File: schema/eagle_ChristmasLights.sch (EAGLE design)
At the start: 3 parts, among them SW1 FSM6JSMA, U1 WS2812

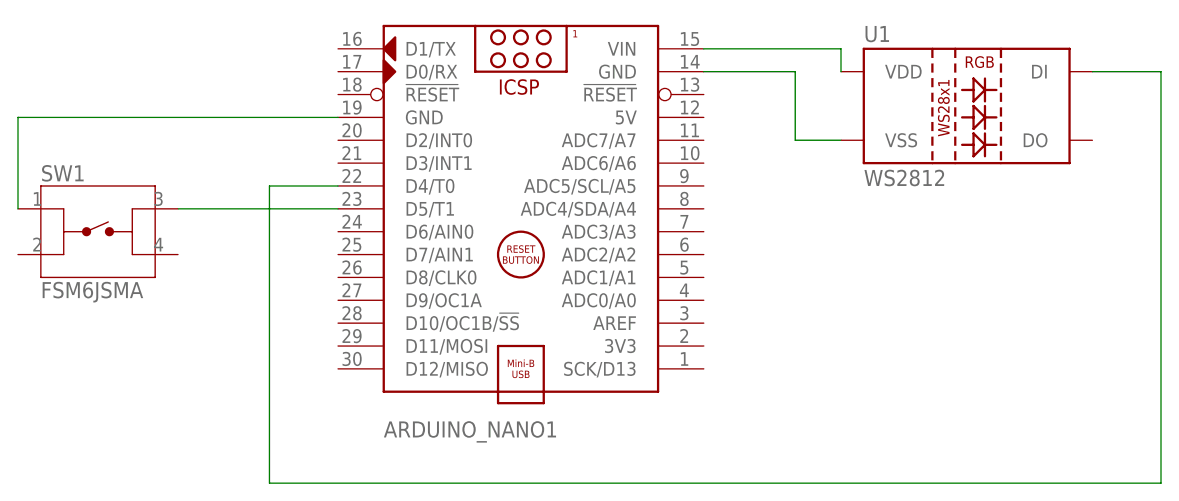
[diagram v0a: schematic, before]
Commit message: Moved I/O D4 and D5 to D6 and D7 for using D4 and D5 with SCL in future projects
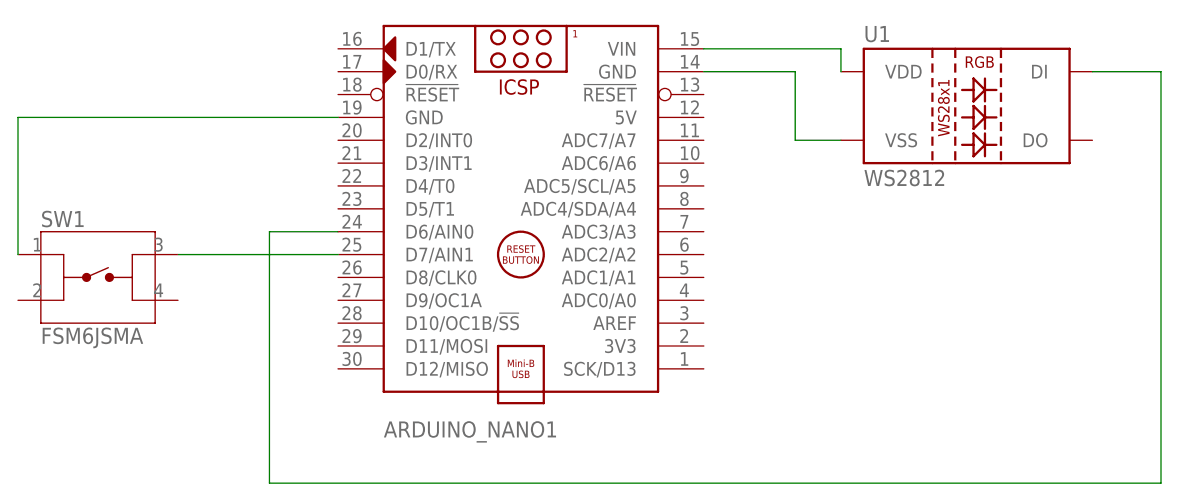
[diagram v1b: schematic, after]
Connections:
- net N$2: now also ARDUINO_NANO1.D7/AIN1; no longer ARDUINO_NANO1.D5/T1
- net N$5: now also ARDUINO_NANO1.D6/AIN0; no longer ARDUINO_NANO1.D4/T0
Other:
- moved on the sheet: SW1
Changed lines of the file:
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@@
 <attribute name="VALUE" x="2.54" y="38.1" size="1.778" layer="96"/>
 </instance>
-<instance part="SW1" gate="G$1" x="-27.94" y="63.5" smashed="yes">
-<attribute name="NAME" x="-35.57291875" y="69.09746875" size="1.781009375" layer="95"/>
-<attribute name="VALUE" x="-35.574059375" y="56.120409375" size="1.78128125" layer="96"/>
+<instance part="SW1" gate="G$1" x="-27.94" y="58.42" smashed="yes">
+<attribute name="NAME" x="-35.57291875" y="64.01746875" size="1.781009375" layer="95"/>
+<attribute name="VALUE" x="-35.574059375" y="51.040409375" size="1.78128125" layer="96"/>
 </instance>
 <instance part="U1" gate="U1" x="68.58" y="76.2" smashed="yes">
@@
 <pinref part="SW1" gate="G$1" pin="1"/>
 <wire x1="-2.54" y1="76.2" x2="-38.1" y2="76.2" width="0.1524" layer="91"/>
-<wire x1="-38.1" y1="76.2" x2="-38.1" y2="66.04" width="0.1524" layer="91"/>
+<wire x1="-38.1" y1="76.2" x2="-38.1" y2="60.96" width="0.1524" layer="91"/>
 </segment>
 </net>
@@
 <segment>
 <pinref part="SW1" gate="G$1" pin="3"/>
-<pinref part="ARDUINO_NANO1" gate="G$1" pin="D5/T1"/>
-<wire x1="-20.32" y1="66.04" x2="-2.54" y2="66.04" width="0.1524" layer="91"/>
+<pinref part="ARDUINO_NANO1" gate="G$1" pin="D7/AIN1"/>
+<wire x1="-20.32" y1="60.96" x2="-2.54" y2="60.96" width="0.1524" layer="91"/>
 </segment>
 </net>
@@
 <net name="N$5" class="0">
 <segment>
-<pinref part="ARDUINO_NANO1" gate="G$1" pin="D4/T0"/>
-<wire x1="-2.54" y1="68.58" x2="-10.16" y2="68.58" width="0.1524" layer="91"/>
-<wire x1="-10.16" y1="68.58" x2="-10.16" y2="35.56" width="0.1524" layer="91"/>
 <wire x1="-10.16" y1="35.56" x2="88.9" y2="35.56" width="0.1524" layer="91"/>
 <pinref part="U1" gate="U1" pin="DI"/>
 <wire x1="88.9" y1="35.56" x2="88.9" y2="81.28" width="0.1524" layer="91"/>
 <wire x1="88.9" y1="81.28" x2="81.28" y2="81.28" width="0.1524" layer="91"/>
+<wire x1="-10.16" y1="35.56" x2="-10.16" y2="63.5" width="0.1524" layer="91"/>
+<pinref part="ARDUINO_NANO1" gate="G$1" pin="D6/AIN0"/>
+<wire x1="-10.16" y1="63.5" x2="-2.54" y2="63.5" width="0.1524" layer="91"/>
 </segment>
 </net>
